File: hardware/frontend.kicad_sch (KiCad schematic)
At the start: 71 parts, among them U201 BQ769x2

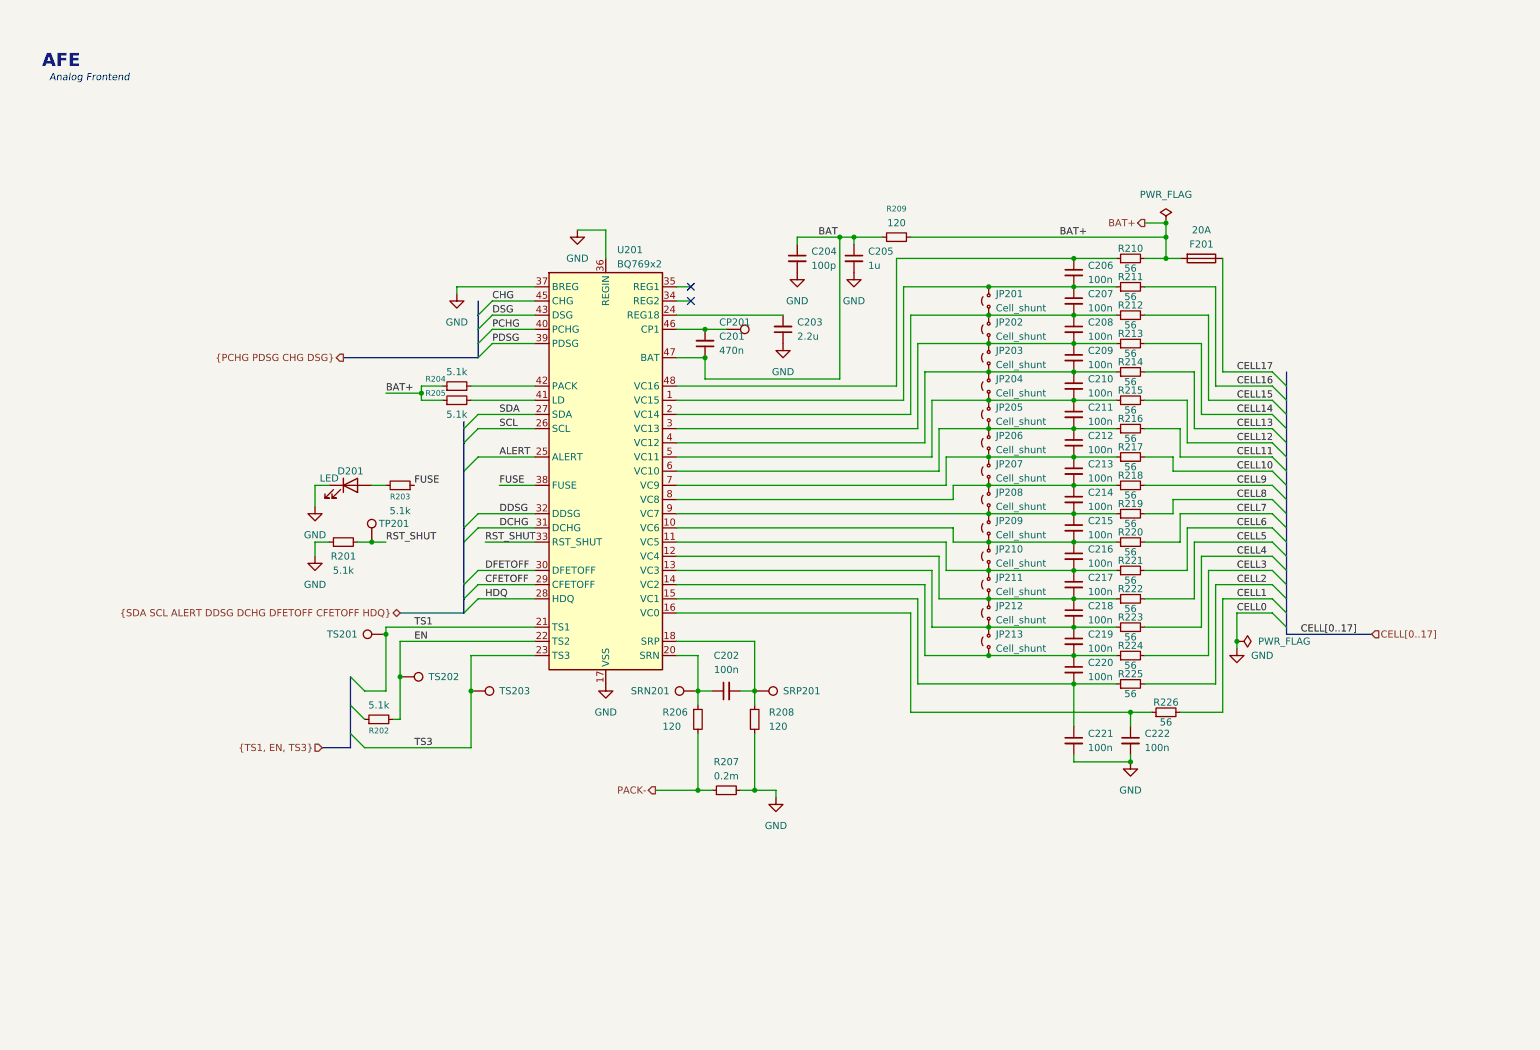
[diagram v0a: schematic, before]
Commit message: add sync folder
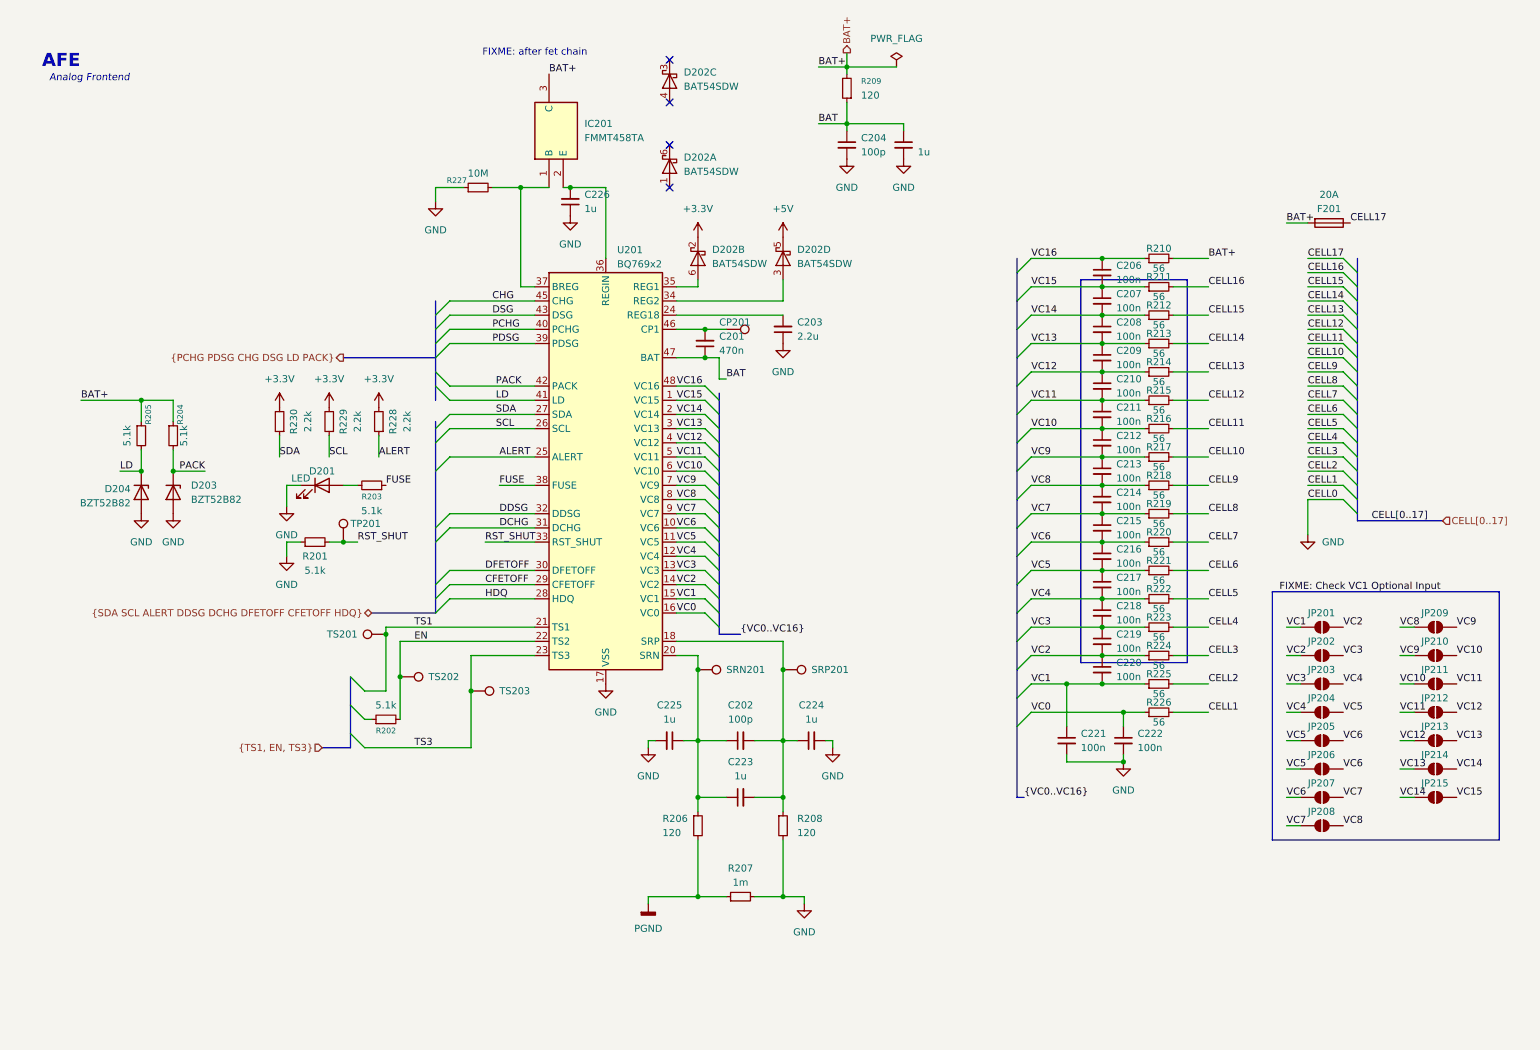
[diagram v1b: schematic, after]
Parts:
- removed JP201, JP202, JP203, JP204, JP205, JP206, JP207, JP208, JP209, JP210, JP211, JP212, JP213: Cell_shunt, Jumper:SolderJumper-2_P1.3mm_Open_Pad1.0x1.5mm, symbol Jumper:Jumper_2_Small_Open
- added C223, C224, C225: 1u, Capacitor_SMD:C_0402_1005Metric, symbol Device:C_Small
- added C226: 1u, Capacitor_SMD:C_0603_1608Metric, symbol Device:C_Small
- added D202: BAT54SDW, Package_TO_SOT_SMD:SOT-363_SC-70-6, symbol Diode:BAT54SDW
- added D203, D204: BZT52B82, Diode_SMD:D_SOD-123F, symbol Diode:BZT52Bxx
- added IC201: FMMT458TA, Samacsys:SOT96P240X110-3N, symbol Samacsys:FMMT458TA
- added JP201, JP202, JP203, JP204, JP205, JP206, JP207, JP208, JP209, JP210, JP211, JP212, JP213, JP214, JP215: SolderJumper_2_Open, symbol Jumper:SolderJumper_2_Open
- added R227: 10M, Resistor_SMD:R_0402_1005Metric, symbol Device:R_Small
- added R228, R229, R230: 2.2k, Resistor_SMD:R_0402_1005Metric, symbol Device:R_Small
- C202: value 100n -> 100p
- R207: value 0.2m -> 1m
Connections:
- net ALERT: now also R228.1
- net BAT+: now also IC201.3 (C)
- net GND: now also C224.2, C225.2, C226.1, D203.2 (A), D204.2 (A), R227.1; no longer U201.36 (REGIN), U201.37 (BREG)
- net SCL: now also R229.1
- net SDA: now also R230.1
- net VC8: now reaches C213.2, C214.1, R218.1, U201.8 (VC8)
- net VC8: now also JP208.1 (A), JP209.2 (B)
- net VC16: now reaches C206.1, R210.1, U201.48 (VC16)
- net VC15: now reaches C206.2, C207.1, R211.1, U201.1 (VC15)
- net VC15: now also JP215.1 (A)
- net VC0: now reaches C222.1, R226.1, U201.16 (VC0)
- net VC9: now reaches C212.2, C213.1, R217.1, U201.7 (VC9)
- net VC9: now also JP209.1 (A), JP210.2 (B)
- net VC13: now reaches C208.2, C209.1, R213.1, U201.3 (VC13)
- net VC13: now also JP213.1 (A), JP214.2 (B)
- net VC14: now reaches C207.2, C208.1, R212.1, U201.2 (VC14)
- net VC14: now also JP214.1 (A), JP215.2 (B)
- net VC3: now reaches C218.2, C219.1, R223.1, U201.13 (VC3)
- net VC3: now also JP202.1 (A), JP203.2 (B)
- net VC4: now reaches C217.2, C218.1, R222.1, U201.12 (VC4)
- net VC4: now also JP203.1 (A), JP204.2 (B)
- net VC10: now reaches C211.2, C212.1, R216.1, U201.6 (VC10)
- net VC10: now also JP210.1 (A), JP211.2 (B)
- net VC11: now reaches C210.2, C211.1, R215.1, U201.5 (VC11)
- net VC11: now also JP211.1 (A), JP212.2 (B)
- net VC5: now reaches C216.2, C217.1, R221.1, U201.11 (VC5)
- net VC5: now also JP204.1 (A), JP205.2 (B), JP206.2 (B)
- net VC12: now reaches C209.2, C210.1, R214.1, U201.4 (VC12)
- net VC12: now also JP212.1 (A), JP213.2 (B)
- net at C202.2, R208.1, SRP201.1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: now also C223.2, C224.1
- net VC6: now reaches C215.2, C216.1, R220.1, U201.10 (VC6)
- net VC6: now also JP205.1 (A), JP206.1 (A), JP207.2 (B)
- net VC7: now reaches C214.2, C215.1, R219.1, U201.9 (VC7)
- net VC7: now also JP207.1 (A), JP208.2 (B)
- net VC2: now reaches C219.2, C220.1, R224.1, U201.14 (VC2)
- net VC2: now also JP201.1 (A), JP202.2 (B)
- net VC1: now reaches C220.2, C221.1, R225.1, U201.15 (VC1)
- net VC1: now also JP201.2 (B)
- net at C202.1, R206.1, SRN201.1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: now also C223.1, C225.1
- net LD: now reaches R205.2, U201.41 (LD)
- net LD: now also D204.1 (K)
- net at U201.34 (REG2): now also D202.3 (A)
- net at U201.35 (REG1): now also D202.6 (A)
- net PACK: now reaches R204.2, U201.42 (PACK)
- net PACK: now also D203.1 (K)
- net PACK- renamed PGND
- new net: IC201.1 (B), R227.2, U201.37 (BREG)
- new net: C226.2, IC201.2 (E), U201.36 (REGIN)
- new net +3.3V: D202.2 (K), R228.2, R229.2, R230.2
- new net +5V: D202.5 (K)
- no-connect marks 2 -> 4
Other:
- note added: "FIXME: after fet chain"
- moved on the sheet: C202, C204, C206, C207, C208, C209, C210, C211, C212, C213, C214, C215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

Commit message: Restore robust hardware project state and clean up test files
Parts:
- removed D203, D204: BZT52B82, Diode_SMD:D_SOD-123F, symbol Diode:BZT52Bxx
- removed F201: 20A, Fuse:Fuse_Littelfuse-NANO2-451_453, symbol Device:Fuse
- removed R204, R205: 5.1k, Resistor_SMD:R_0402_1005Metric, symbol Device:R_Small
- R210, R211, R212, R213, R214, R215, R216, R217, R218, R219, R220, R221, R222, R223, R224, R225, R226: value 56 -> 100
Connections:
- net BAT+: no longer IC201.3 (C), R210.2
- net CELL17: now also R210.2
- new net CH: IC201.3 (C)
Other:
- note removed: "FIXME: after fet chain"
- moved on the sheet: C226, D202A, D202C, IC201, R227, TS201

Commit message: add fuses
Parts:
- added JP1: SJ3O, symbol Jumper:SolderJumper_3_Open
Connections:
- net FUSE: now also JP1.2 (C), JP1.3 (B); no longer R203.1
- net GND: now also R203.2; no longer D201.1 (K)
- net at D201.2 (A): now also JP1.1 (A); no longer R203.2
- new net: D201.1 (K), R203.1
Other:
- note added: "<-- Current --"
- moved on the sheet: D201, R201, R203, TP201

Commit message: improve fuse connectios
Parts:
- removed R202: 5.1k, Resistor_SMD:R_0402_1005Metric, symbol Device:R_Small
- added Q2: 2N7002, Package_TO_SOT_SMD:SOT-23, symbol Transistor_FET:2N7002
- added R204: 50k, Resistor_SMD:R_0402_1005Metric, symbol Device:R_Small
- added R235: 120, Resistor_SMD:R_0402_1005Metric, symbol Device:R_Small
- added TS204, TS205, TS206: TestPoint, TestPoint:TestPoint_Pad_D1.0mm, symbol Connector:TestPoint
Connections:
- net DDSG is gone; now on net ALERT: U201.32 (DDSG)
- net ALERT: no longer U201.25 (ALERT)
- net GND: now also Q2.2 (S), R204.2
- net SCL: no longer U201.26 (SCL)
- net SDA: no longer U201.27 (SDA)
- net CFETOFF renamed TS6
- net TS6: now also TS206.1
- net DCHG renamed TS4
- net TS4: now also TS204.1
- net DFETOFF renamed TS5
- net TS5: now also TS205.1
- net EN renamed TS2
- net TS2: now also Q2.3 (D)
- net HDQ renamed SPI.CS
- new net: Q2.1 (G), R235.1
- new net SPI.MISO: U201.25 (ALERT)
- new net SPI.MOSI: U201.27 (SDA)
- new net SPI.SCLK: U201.26 (SCL)
- new net WAKE: R204.1, R235.2
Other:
- note added: "Used also as Wake UP"
- moved on the sheet: D201, JP1, R201, R203, TP201

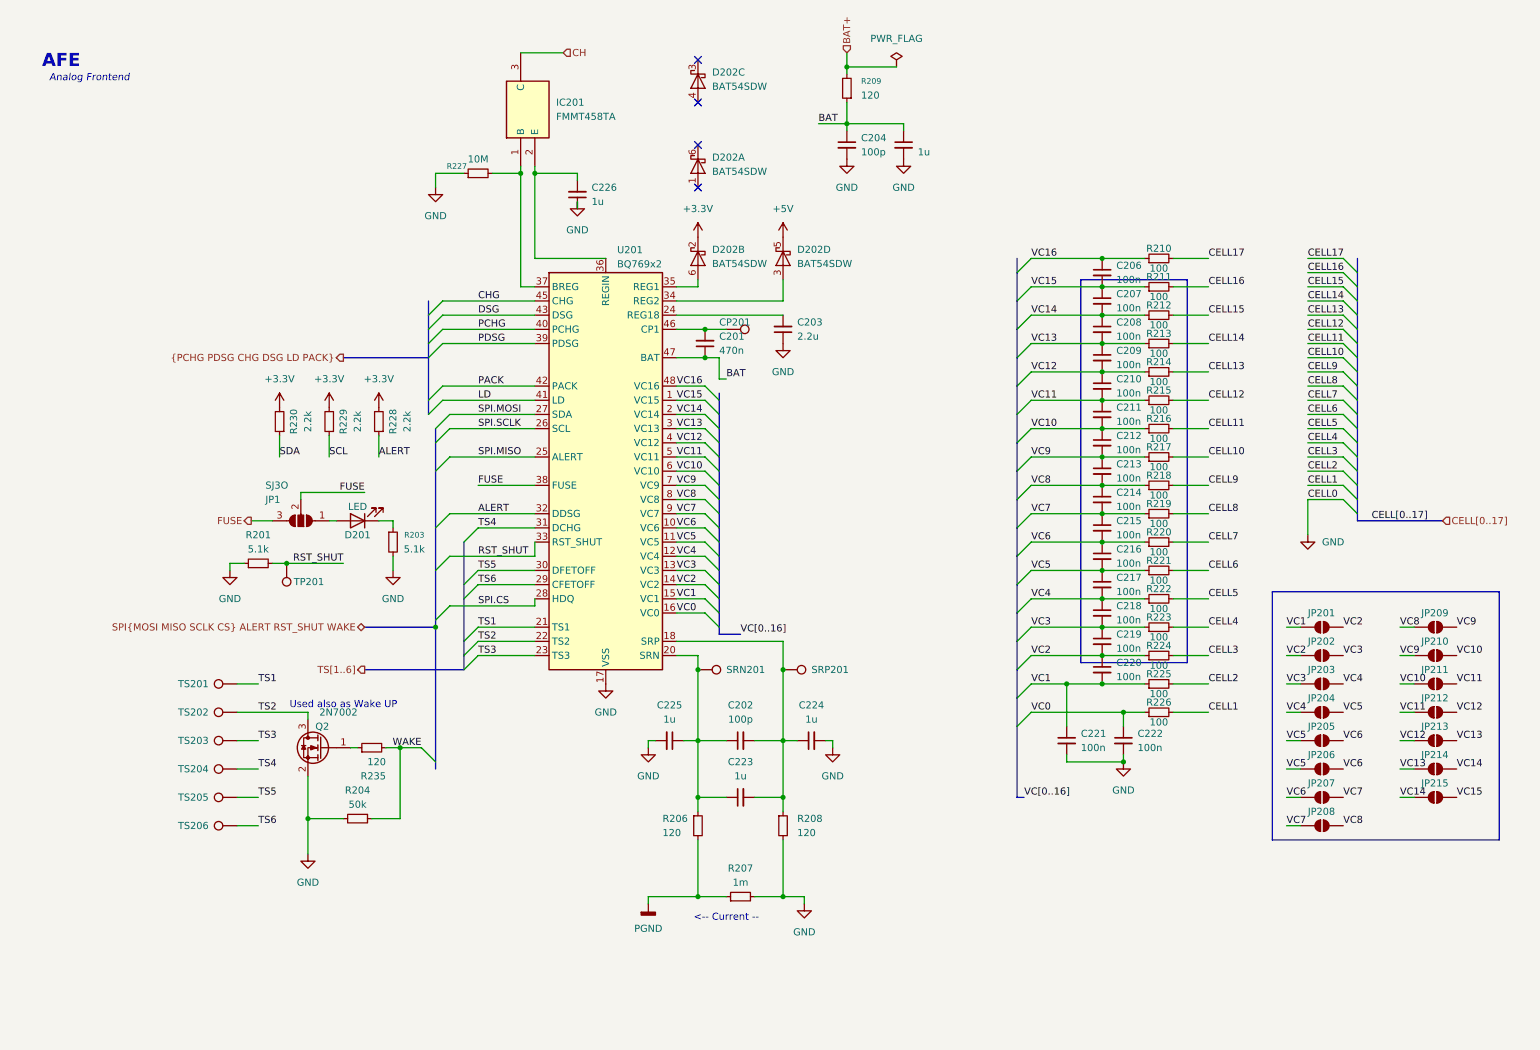
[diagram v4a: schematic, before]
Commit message: remove jetbrains mcps, add uv in home and update flake
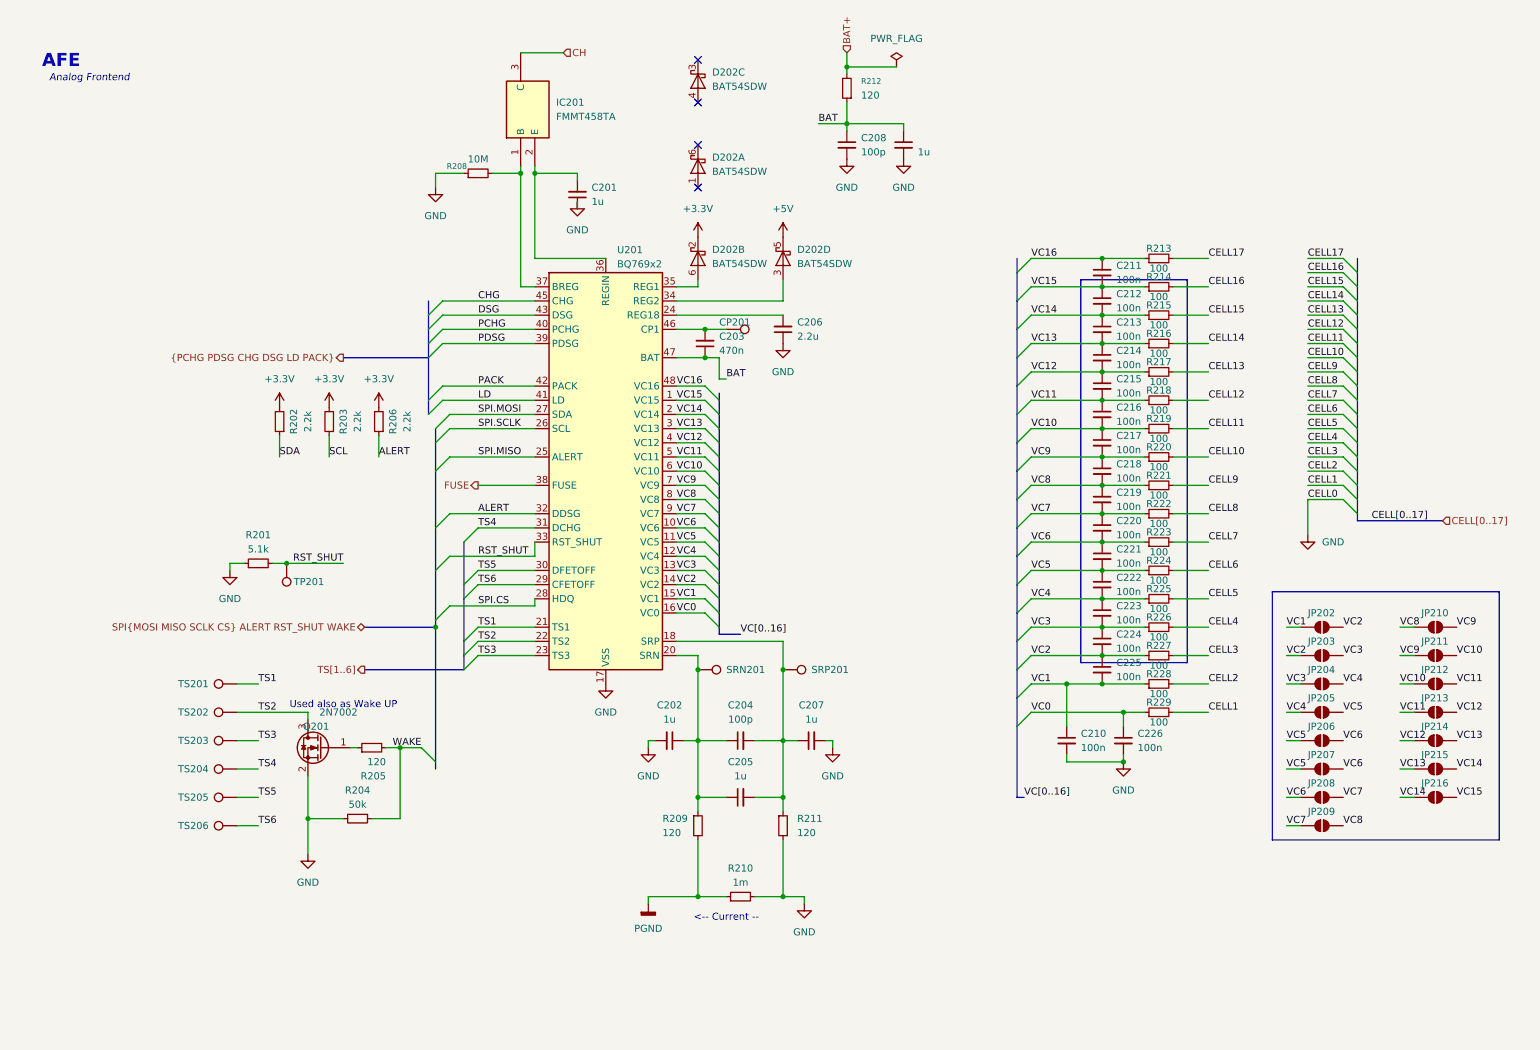
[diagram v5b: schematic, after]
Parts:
- removed D201: LED, LED_THT:LED_D3.0mm, symbol Device:LED
- removed JP1: SJ3O, symbol Jumper:SolderJumper_3_Open
- removed R203: 5.1k, Resistor_SMD:R_0402_1005Metric, symbol Device:R_Small
- renumbered C226 to C201, C225 to C202, C201 to C203, C202 to C204, C223 to C205, C203 to C206, C224 to C207, C204 to C208, C205 to C209, C221 to C210, C206 to C211, C207 to C212, C208 to C213, C209 to C214, C210 to C215, C211 to C216, C212 to C217, C213 to C218, C214 to C219, C215 to C220, C216 to C221, C217 to C222, C218 to C223, C219 to C224, C220 to C225, C222 to C226, JP201 to JP202, JP202 to JP203, JP203 to JP204, JP204 to JP205, JP205 to JP206, JP206 to JP207, JP207 to JP208, JP208 to JP209, JP209 to JP210, JP210 to JP211, JP211 to JP212, JP212 to JP213, JP213 to JP214, JP214 to JP215, JP215 to JP216, Q2 to Q201, R230 to R202, R229 to R203, R235 to R205, R228 to R206, R227 to R208, R206 to R209, R207 to R210, R208 to R211, R209 to R212, R210 to R213, R211 to R214, R212 to R215, R213 to R216, R214 to R217, R215 to R218, R216 to R219, R217 to R220, R218 to R221, R219 to R222, R220 to R223, R221 to R224, R222 to R225, R223 to R226, R224 to R227, R225 to R228, R226 to R229

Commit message: change props
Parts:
- C201, C203, C206, C208: footprint Capacitor_SMD:C_0603_1608Metric -> Capacitor_SMD:C_0805_2012Metric
- C202, C204, C205, C207, C210, C211, C212, C213, C214, C215, C216, C217, C218, C219, C220, C221, C222, C223, C224, C225, C226: footprint Capacitor_SMD:C_0402_1005Metric -> Capacitor_SMD:C_0805_2012Metric
- R201, R202, R203, R204, R205, R206: footprint Resistor_SMD:R_0402_1005Metric -> Resistor_SMD:R_0805_2012Metric
- R207: renamed from R208; footprint Resistor_SMD:R_0402_1005Metric -> Resistor_SMD:R_0805_2012Metric
- R208: renamed from R209; footprint Resistor_SMD:R_0402_1005Metric -> Resistor_SMD:R_0805_2012Metric
- R210: renamed from R211; footprint Resistor_SMD:R_0402_1005Metric -> Resistor_SMD:R_0805_2012Metric
- R211: renamed from R212; footprint Resistor_SMD:R_0402_1005Metric -> Resistor_SMD:R_0805_2012Metric
- renumbered D202 to D201, JP202 to JP201, JP203 to JP202, JP204 to JP203, JP205 to JP204, JP206 to JP205, JP207 to JP206, JP208 to JP207, JP209 to JP208, JP210 to JP209, JP211 to JP210, JP212 to JP211, JP213 to JP212, JP214 to JP213, JP215 to JP214, JP216 to JP215, R210 to R209, R213 to R212, R214 to R213, R215 to R214, R216 to R215, R217 to R216, R218 to R217, R219 to R218, R220 to R219, R221 to R220, R222 to R221, R223 to R222, R224 to R223, R225 to R224, R226 to R225, R227 to R226, R228 to R227, R229 to R228
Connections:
- net TS6 is gone; now on net TS5: TS206.1, U201.29 (CFETOFF)
- net TS2: now also TS203.1, U201.23 (TS3); no longer Q201.3 (D), TS202.1, U201.22 (TS2)
- net TS3: now also TS204.1, U201.31 (DCHG); no longer TS203.1, U201.23 (TS3)
- net TS4: now also TS205.1, U201.30 (DFETOFF); no longer TS204.1, U201.31 (DCHG)
- net TS5: no longer TS205.1, U201.30 (DFETOFF)
- net SPI.CS renamed SPI.CFETOFF
- net SPI.MISO renamed SPI.SDA
- net SPI.MOSI renamed SPI.HDQ
- net SPI.SCLK renamed SPI.SCL
- new net TS2_W: Q201.3 (D), TS202.1, U201.22 (TS2)
